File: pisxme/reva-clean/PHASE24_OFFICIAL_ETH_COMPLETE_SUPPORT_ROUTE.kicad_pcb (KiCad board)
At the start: 6 copper layers, 300 x 180 mm, 103 parts, among them J1 74221-101LF, J2 A70-112-331N126, J3 JAE SM3ZS067U410ABR1000 B-key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, J4 Amphenol 10171746-00021LF USB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, J5 0039300020, J6 0039300020, J7 Raspberry-Pi-5-Compute-Module, Q1 CSD19536KCS, Q2 CSD19536KCS, U1 LM74700QDBVRQ1, U2 LM74700QDBVRQ1, U3 TPSM63606RDLR, U4 TPSM63606RDLR, U5 TPSM63606RDLR, U6 TPD4EUSB30, U7 TUSB9261IPVP, U8 Texas_DRT_3, U9 TPD4EUSB30

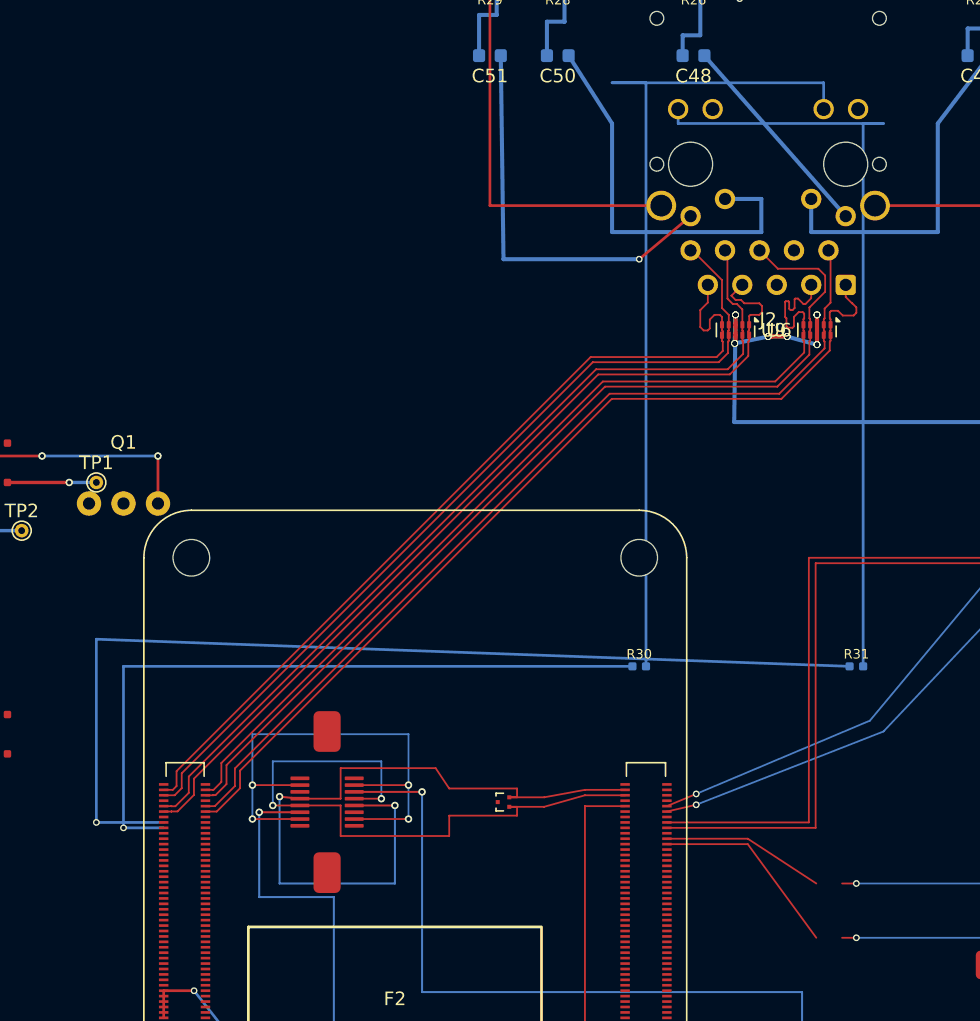
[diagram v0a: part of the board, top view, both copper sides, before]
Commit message: phase24: reject mixed-side Ethernet LED probe
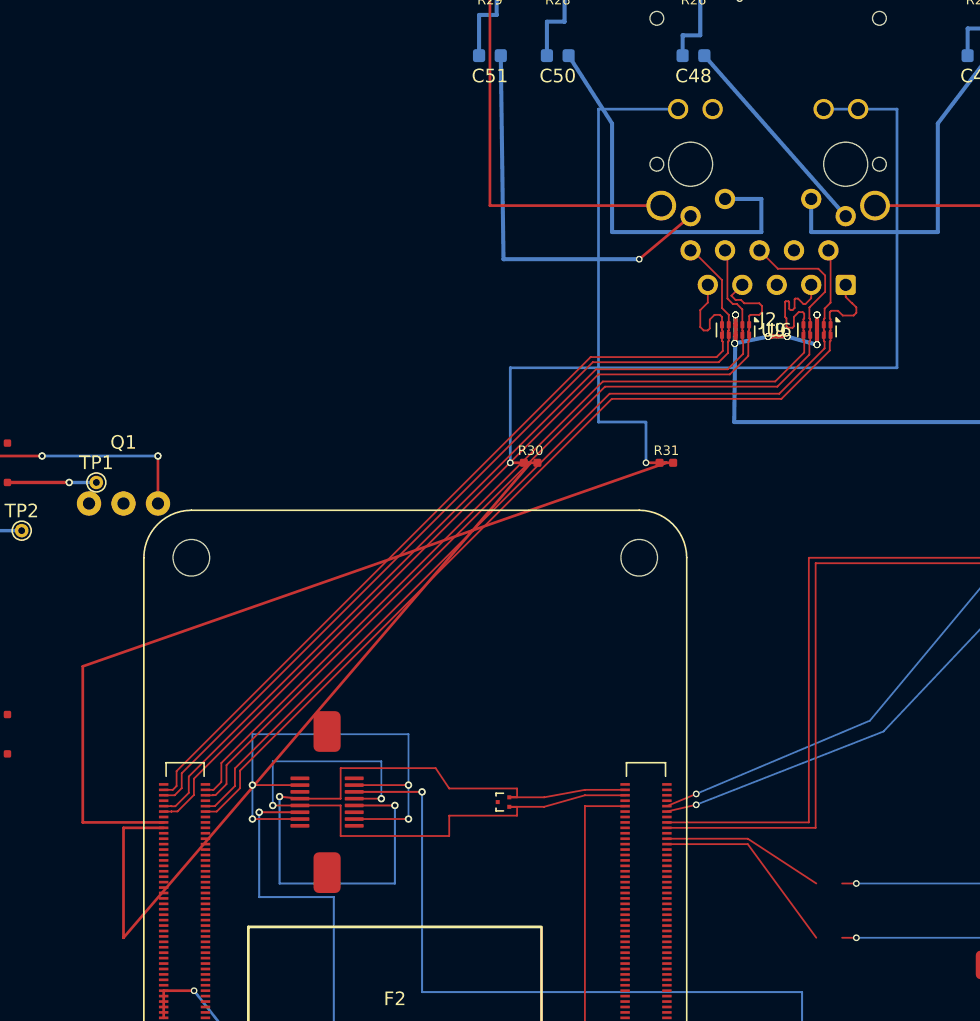
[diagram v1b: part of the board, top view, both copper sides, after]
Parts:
- R30, R31: moved to F.Cu
- moved R31 20.5 mm to (70.0, 75.0)
- moved R30 17.0 mm to (60.0, 75.0)
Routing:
- net /ETHERNET/GBE_LED_G_K: track 57.7 -> 37.4 mm, vias 0 -> 1
- net ETH_LEDG: track 74.0 -> 63.5 mm, vias 1 -> 0
- net ETH_LEDY: track 52.4 -> 57.7 mm, vias 1 -> 0
- net /ETHERNET/GBE_LED_Y_K: track 63.0 -> 62.0 mm, vias 0 -> 1

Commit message: phase24: reject J2-west Ethernet LED probe
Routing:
- net ETH_LEDY: track 57.7 -> 128.3 mm, vias 0 -> 1
- net ETH_LEDG: track 63.5 -> 127.3 mm, vias 0 -> 1
- net /ETHERNET/GBE_LED_Y_K: track 62.0 -> 46.5 mm, vias 1 -> 0
- net /ETHERNET/GBE_LED_G_K: track 37.4 -> 34.3 mm, vias 1 -> 0

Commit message: phase24: reject J7-west Ethernet LED probe
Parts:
- moved R31 52.4 mm to (24.0, 100.0)
- moved R30 45.6 mm to (24.0, 103.0)
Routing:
- net ETH_LEDY: track 128.3 -> 9.66 mm, vias 1 -> 0
- net ETH_LEDG: track 127.3 -> 9.81 mm, vias 1 -> 0
- net /ETHERNET/GBE_LED_G_K: track 34.3 -> 146.7 mm, vias 0 -> 1
- net /ETHERNET/GBE_LED_Y_K: track 46.5 -> 152.4 mm, vias 0 -> 1

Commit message: phase24: reject rotated Ethernet LED probe
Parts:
- moved R31 7.21 mm to (20.0, 106.0), turned to 90 degrees
- moved R30 3.00 mm to (24.0, 106.0), turned to 90 degrees
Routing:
- net /ETHERNET/GBE_LED_G_K: track 146.7 -> 160.4 mm
- net /ETHERNET/GBE_LED_Y_K: track 152.4 -> 161.1 mm
- net ETH_LEDG: track 9.81 -> 14.3 mm
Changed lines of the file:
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@@
 	(footprint "R_0402_1005Metric"
 		(layer "F.Cu")
-		(at 246 118)
+		(at 20 106 90)
 		(descr "IPC-7351 nominal 0402 resistor; 1.00 x 0.50 mm body; clean-project commodity passive")
-		(property "Reference" "R20"
-			(at 0 -0.9 0)
+		(property "Reference" "R31"
+			(at 0 -0.9 90)
 			(layer "F.SilkS")
 			(effects
@@
 		)
 		(property "Value" "R_0402_1005Metric"
-			(at 0 0.9 0)
+			(at 0 0.9 90)
 			(layer "F.Fab")
 			(hide yes)
@@
 		)
 		(property "Datasheet" ""
-			(at 0 0 0)
+			(at 0 0 90)
 			(layer "F.Fab")
 			(hide yes)
@@
 		)
 		(property "Description" ""
-			(at 0 0 0)
+			(at 0 0 90)
 			(layer "F.Fab")
 			(hide yes)
@@
 		)
 		(pad "1" smd roundrect
-			(at -0.5 0)
+			(at -0.5 0 90)
 			(size 0.6 0.6)
 			(layers "F.Cu" "F.Mask" "F.Paste")
 			(roundrect_rratio 0.2)
-			(net "/REGULATORS/FB_BRIDGE_1V1")
+			(net "ETH_LEDG")
 		)
 		(pad "2" smd roundrect
-			(at 0.5 0)
+			(at 0.5 0 90)
 			(size 0.6 0.6)
 			(layers "F.Cu" "F.Mask" "F.Paste")
 			(roundrect_rratio 0.2)
-			(net "POWER_GND")
+			(net "/ETHERNET/GBE_LED_G_K")
 		)
 		(embedded_fonts no)
@@
 	(footprint "R_0402_1005Metric"
 		(layer "F.Cu")
-		(at 24 100)
+		(at 246 118)
 		(descr "IPC-7351 nominal 0402 resistor; 1.00 x 0.50 mm body; clean-project commodity passive")
-		(property "Reference" "R31"
+		(property "Reference" "R20"
 			(at 0 -0.9 0)
 			(layer "F.SilkS")
@@
 			(layers "F.Cu" "F.Mask" "F.Paste")
 			(roundrect_rratio 0.2)
-			(net "ETH_LEDG")
+			(net "/REGULATORS/FB_BRIDGE_1V1")
 		)
 		(pad "2" smd roundrect
@@
 			(layers "F.Cu" "F.Mask" "F.Paste")
 			(roundrect_rratio 0.2)
-			(net "/ETHERNET/GBE_LED_G_K")
+			(net "POWER_GND")
 		)
 		(embedded_fonts no)
@@
 		(embedded_fonts no)
 	)
-	(footprint "R_0402_1005Metric"
-		(layer "F.Cu")
-		(at 24 103)
-		(descr "IPC-7351 nominal 0402 resistor; 1.00 x 0.50 mm body; clean-project commodity passive")
-		(property "Reference" "R30"
-			(at 0 -0.9 0)
-			(layer "F.SilkS")
-			(effects
-				(font
-					(size 0.7 0.7)
-					(thickness 0.12)
-				)
-			)
-		)
-		(property "Value" "R_0402_1005Metric"
-			(at 0 0.9 0)
-			(layer "F.Fab")
-			(hide yes)
-			(effects
-				(font
-					(size 0.7 0.7)
-					(thickness 0.12)
-				)
-			)
-		)
-		(property "Datasheet" ""
-			(at 0 0 0)
-			(layer "F.Fab")
-			(hide yes)
-			(effects
-				(font
-					(size 1.27 1.27)
-				)
-			)
-		)
-		(property "Description" ""
-			(at 0 0 0)
-			(layer "F.Fab")
-			(hide yes)
-			(effects
-				(font
-					(size 1.27 1.27)
-				)
-			)
-		)
-		(attr smd)
-		(duplicate_pad_numbers_are_jumpers no)
-		(fp_rect
-			(start -0.7 -0.45)
-			(end 0.7 0.45)
-			(stroke
-				(width 0.05)
-				(type default)
-			)
-			(fill no)
-			(layer "F.CrtYd")
-		)
-		(pad "1" smd roundrect
-			(at -0.5 0)
-			(size 0.6 0.6)
-			(layers "F.Cu" "F.Mask" "F.Paste")
-			(roundrect_rratio 0.2)
-			(net "ETH_LEDY")
-		)
-		(pad "2" smd roundrect
-			(at 0.5 0)
-			(size 0.6 0.6)
-			(layers "F.Cu" "F.Mask" "F.Paste")
-			(roundrect_rratio 0.2)
-			(net "/ETHERNET/GBE_LED_Y_K")
-		)
-		(embedded_fonts no)
-	)
 	(footprint "LM74700QDBVRQ1_SOT23_6"
 		(layer "F.Cu")
@@
 		(embedded_fonts no)
 	)
+	(footprint "R_0402_1005Metric"
+		(layer "F.Cu")
+		(at 24 106 90)
+		(descr "IPC-7351 nominal 0402 resistor; 1.00 x 0.50 mm body; clean-project commodity passive")
+		(property "Reference" "R30"
+			(at 0 -0.9 90)
+			(layer "F.SilkS")
+			(effects
+				(font
+					(size 0.7 0.7)
+					(thickness 0.12)
+				)
+			)
+		)
+		(property "Value" "R_0402_1005Metric"
+			(at 0 0.9 90)
+			(layer "F.Fab")
+			(hide yes)
+			(effects
+				(font
+					(size 0.7 0.7)
+					(thickness 0.12)
+				)
+			)
+		)
+		(property "Datasheet" ""
+			(at 0 0 90)
+			(layer "F.Fab")
+			(hide yes)
+			(effects
+				(font
+					(size 1.27 1.27)
+				)
+			)
+		)
+		(property "Description" ""
+			(at 0 0 90)
+			(layer "F.Fab")
+			(hide yes)
+			(effects
+				(font
+					(size 1.27 1.27)
+				)
+			)
+		)
+		(attr smd)
+		(duplicate_pad_numbers_are_jumpers no)
+		(fp_rect
+			(start -0.7 -0.45)
+			(end 0.7 0.45)
+			(stroke
+				(width 0.05)
+				(type default)
+			)
+			(fill no)
+			(layer "F.CrtYd")
+		)
+		(pad "1" smd roundrect
+			(at -0.5 0 90)
+			(size 0.6 0.6)
+			(layers "F.Cu" "F.Mask" "F.Paste")
+			(roundrect_rratio 0.2)
+			(net "ETH_LEDY")
+		)
+		(pad "2" smd roundrect
+			(at 0.5 0 90)
+			(size 0.6 0.6)
+			(layers "F.Cu" "F.Mask" "F.Paste")
+			(roundrect_rratio 0.2)
+			(net "/ETHERNET/GBE_LED_Y_K")
+		)
+		(embedded_fonts no)
+	)
 	(footprint "TPSM63606RDLR_RDL0020"
 		(layer "F.Cu")
@@
 	)
 	(segment
-		(start 22 106)
-		(end 24.5 103)
+		(start 81.59 48.94)
+		(end 79 48.94)
+		(width 0.2)
+		(layer "F.Cu")
+		(net "/ETHERNET/GBE_LED_Y_K")
+	)
+	(segment
+		(start 27 109)
+		(end 24 105.5)
 		(width 0.2)
 		(layer "F.Cu")
@@
 	)
 	(via
-		(at 22 106)
+		(at 27 109)
 		(size 0.5)
 		(drill 0.3)
@@
 	)
 	(segment
-		(start 10 106)
-		(end 22 106)
+		(start 10 45)
+		(end 10 109)
 		(width 0.2)
 		(layer "B.Cu")
@@
 	)
 	(segment
-		(start 79 48.94)
-		(end 79 45)
+		(start 79 45)
+		(end 10 45)
 		(width 0.2)
 		(layer "B.Cu")
@@
 	)
 	(segment
-		(start 81.59 48.94)
-		(end 79 48.94)
+		(start 79 48.94)
+		(end 79 45)
 		(width 0.2)
 		(layer "B.Cu")
@@
 	)
 	(segment
-		(start 10 45)
-		(end 10 106)
+		(start 10 109)
+		(end 27 109)
 		(width 0.2)
 		(layer "B.Cu")
@@
 	)
 	(segment
-		(start 79 45)
-		(end 10 45)
+		(start 70.87 48.94)
+		(end 68 48.94)
 		(width 0.2)
-		(layer "B.Cu")
-		(net "/ETHERNET/GBE_LED_Y_K")
+		(layer "F.Cu")
+		(net "/ETHERNET/GBE_LED_G_K")
 	)
 	(segment
-		(start 22 97)
-		(end 24.5 100)
+		(start 23 109)
+		(end 20 105.5)
 		(width 0.2)
 		(layer "F.Cu")
@@
 	)
 	(via
-		(at 22 97)
+		(at 23 109)
 		(size 0.5)
 		(drill 0.3)
@@
 	)
 	(segment
-		(start 68 48.94)
-		(end 68 40)
-		(width 0.2)
-		(layer "B.Cu")
-		(net "/ETHERNET/GBE_LED_G_K")
-	)
-	(segment
-		(start 8 40)
-		(end 8 97)
+		(start 8 109)
+		(end 23 109)
 		(width 0.2)
 		(layer "B.Cu")
@@
 	)
 	(segment
-		(start 70.87 48.94)
-		(end 68 48.94)
+		(start 68 40)
+		(end 8 40)
 		(width 0.2)
 		(layer "B.Cu")
@@
 	)
 	(segment
-		(start 68 40)
-		(end 8 40)
+		(start 8 40)
+		(end 8 109)
 		(width 0.2)
 		(layer "B.Cu")
@@
 	)
 	(segment
-		(start 8 97)
-		(end 22 97)
+		(start 68 48.94)
+		(end 68 40)
 		(width 0.2)
 		(layer "B.Cu")
@@
 	)
 	(segment
-		(start 32.96 101.9)
-		(end 30 101.9)
+		(start 27 104)
+		(end 24 105.5)
 		(width 0.2)
 		(layer "F.Cu")
@@
 	)
 	(segment
-		(start 27 103)
-		(end 23.5 103)
+		(start 32.96 101.9)
+		(end 30 101.9)
 		(width 0.2)
 		(layer "F.Cu")
@@
 	(segment
 		(start 30 101.9)
-		(end 27 103)
+		(end 27 104)
 		(width 0.2)
 		(layer "F.Cu")
@@
 	(segment
 		(start 32.96 101.5)
-		(end 30 101.5)
+		(end 29 101.5)
 		(width 0.2)
 		(layer "F.Cu")
@@
 	)
 	(segment
-		(start 27 100)
-		(end 23.5 100)
+		(start 29 101.5)
+		(end 24 102)
 		(width 0.2)
 		(layer "F.Cu")
@@
 	)
 	(segment
-		(start 30 101.5)
-		(end 27 100)
+		(start 24 102)
+		(end 20 105.5)
 		(width 0.2)
 		(layer "F.Cu")
